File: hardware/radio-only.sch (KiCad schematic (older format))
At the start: 22 parts, among them P1 CONN_2, P2 CONN_2, P3 CONN_4, U3 AT86RF231, Y1 NX3225SA-16MHz-15ppm

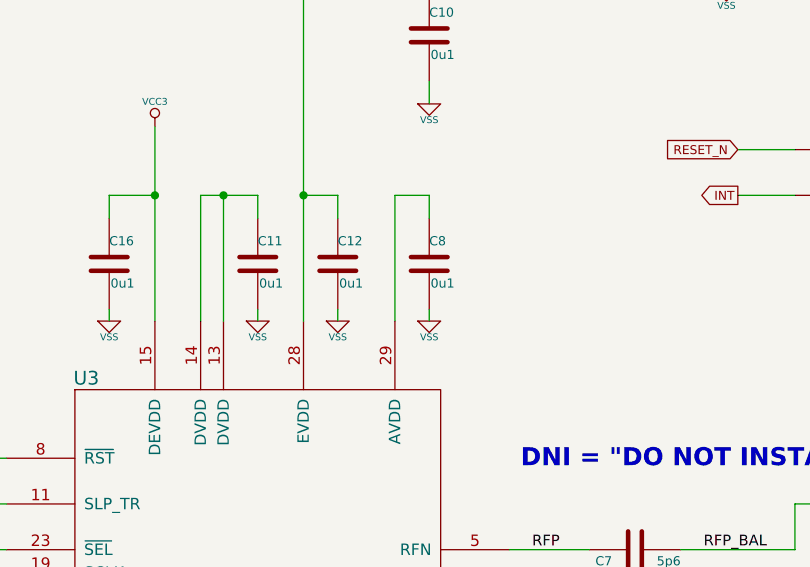
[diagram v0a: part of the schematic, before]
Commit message: Corrections to C8/12 decoupling caps. Should be 0u01, not 0u1 (not critical).
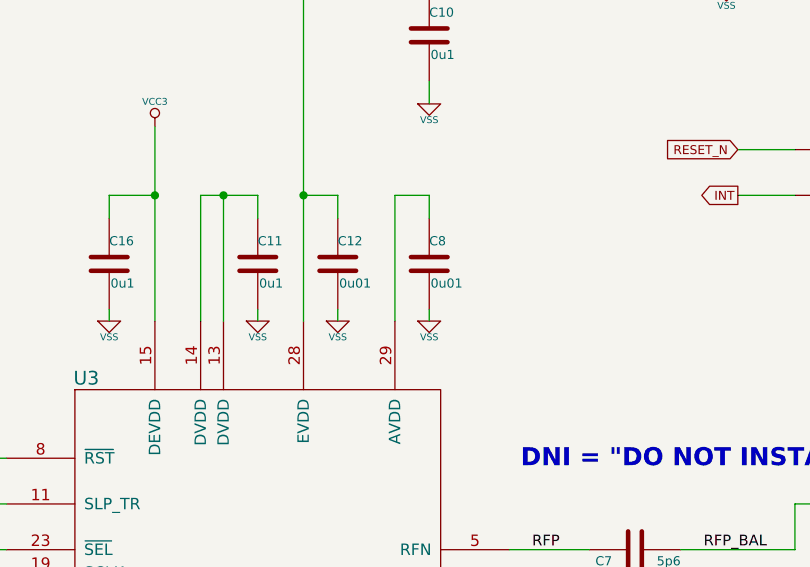
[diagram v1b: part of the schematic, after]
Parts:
- C12, C8: value 0u1 -> 0u01
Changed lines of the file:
@@
 Sheet 1 1
 Title "FREAKDUINO-CHIBI 2.4GHz"
-Date "14 feb 2014"
+Date "3 mar 2014"
 Rev "v1.2"
 Comp "KiCAD version by Gruvin"
@@
 P 4850 2750
 F 0 "C12" H 4850 2850 40  0000 L CNN
-F 1 "0u1" H 4856 2665 40  0000 L CNN
+F 1 "0u01" H 4856 2665 40  0000 L CNN
 F 2 "" H 4888 2600 30  0000 C CNN
 F 3 "" H 4850 2750 60  0000 C CNN
@@
 P 5250 2750
 F 0 "C8" H 5250 2850 40  0000 L CNN
-F 1 "0u1" H 5256 2665 40  0000 L CNN
+F 1 "0u01" H 5256 2665 40  0000 L CNN
 F 2 "" H 5288 2600 30  0000 C CNN
 F 3 "" H 5250 2750 60  0000 C CNN

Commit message: Changed the radio test board a) to lie on its side and b) to include slp_tr (oops).
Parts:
- P2: value CONN_2 -> CONN_3; symbol CONN_2 -> CONN_3
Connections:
- net INT: now also P2.3 (P3); no longer P2.2 (PM)
- net RESET_N: now also P2.2 (PM); no longer P2.1 (P1)
- net SLP_TR: now also P2.1 (P1)
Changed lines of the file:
@@
 $EndComp
 $Comp
-L VCC3 #PWR4
+L VCC3 #PWR01
 U 1 1 51E3885A
 P 3500 1200
-F 0 "#PWR4" H 3500 1340 20  0001 C CNN
+F 0 "#PWR01" H 3500 1340 20  0001 C CNN
 F 1 "VCC3" H 3500 1310 30  0000 C CNN
 F 2 "" H 3500 1200 60  0000 C CNN
@@
 $EndComp
 $Comp
-L VCC3 #PWR7
+L VCC3 #PWR02
 U 1 1 51E383F6
 P 4050 2150
-F 0 "#PWR7" H 4050 2290 20  0001 C CNN
+F 0 "#PWR02" H 4050 2290 20  0001 C CNN
 F 1 "VCC3" H 4050 2260 30  0000 C CNN
 F 2 "" H 4050 2150 60  0000 C CNN
@@
 $EndComp
 $Comp
-L VSS #PWR8
+L VSS #PWR03
 U 1 1 51E38434
 P 4500 3000
-F 0 "#PWR8" H 4500 3000 30  0001 C CNN
+F 0 "#PWR03" H 4500 3000 30  0001 C CNN
 F 1 "VSS" H 4500 2930 30  0000 C CNN
 F 2 "" H 4500 3000 60  0000 C CNN
@@
 $EndComp
 $Comp
-L VSS #PWR10
+L VSS #PWR04
 U 1 1 51E3856B
 P 4850 3000
-F 0 "#PWR10" H 4850 3000 30  0001 C CNN
+F 0 "#PWR04" H 4850 3000 30  0001 C CNN
 F 1 "VSS" H 4850 2930 30  0000 C CNN
 F 2 "" H 4850 3000 60  0000 C CNN
@@
 $EndComp
 $Comp
-L VSS #PWR12
+L VSS #PWR05
 U 1 1 51E3859B
 P 5250 3000
-F 0 "#PWR12" H 5250 3000 30  0001 C CNN
+F 0 "#PWR05" H 5250 3000 30  0001 C CNN
 F 1 "VSS" H 5250 2930 30  0000 C CNN
 F 2 "" H 5250 3000 60  0000 C CNN
@@
 $EndComp
 $Comp
-L VSS #PWR6
+L VSS #PWR06
 U 1 1 51E385BF
 P 3850 6050
-F 0 "#PWR6" H 3850 6050 30  0001 C CNN
+F 0 "#PWR06" H 3850 6050 30  0001 C CNN
 F 1 "VSS" H 3850 5980 30  0000 C CNN
 F 2 "" H 3850 6050 60  0000 C CNN
@@
 $EndComp
 $Comp
-L VSS #PWR9
+L VSS #PWR07
 U 1 1 51E385C5
 P 4600 6050
-F 0 "#PWR9" H 4600 6050 30  0001 C CNN
+F 0 "#PWR07" H 4600 6050 30  0001 C CNN
 F 1 "VSS" H 4600 5980 30  0000 C CNN
 F 2 "" H 4600 6050 60  0000 C CNN
@@
 $EndComp
 $Comp
-L VSS #PWR1
+L VSS #PWR08
 U 1 1 51E39377
 P 1050 5850
-F 0 "#PWR1" H 1050 5850 30  0001 C CNN
+F 0 "#PWR08" H 1050 5850 30  0001 C CNN
 F 1 "VSS" H 1050 5780 30  0000 C CNN
 F 2 "" H 1050 5850 60  0000 C CNN
@@
 $EndComp
 $Comp
-L VSS #PWR2
+L VSS #PWR09
 U 1 1 51E3937D
 P 1850 5850
-F 0 "#PWR2" H 1850 5850 30  0001 C CNN
+F 0 "#PWR09" H 1850 5850 30  0001 C CNN
 F 1 "VSS" H 1850 5780 30  0000 C CNN
 F 2 "" H 1850 5850 60  0000 C CNN
@@
 $EndComp
 $Comp
-L VCC3 #PWR3
+L VCC3 #PWR010
 U 1 1 51E39903
 P 2950 2500
-F 0 "#PWR3" H 2950 2640 20  0001 C CNN
+F 0 "#PWR010" H 2950 2640 20  0001 C CNN
 F 1 "VCC3" H 2950 2610 30  0000 C CNN
 F 2 "" H 2950 2500 60  0000 C CNN
@@
 ANT
 $Comp
-L VSS #PWR17
+L VSS #PWR011
 U 1 1 51E3A542
 P 8500 4500
-F 0 "#PWR17" H 8500 4500 30  0001 C CNN
+F 0 "#PWR011" H 8500 4500 30  0001 C CNN
 F 1 "VSS" H 8500 4430 30  0000 C CNN
 F 2 "" H 8500 4500 60  0000 C CNN
@@
 $EndComp
 $Comp
-L VSS #PWR18
+L VSS #PWR012
 U 1 1 51E3A548
 P 9400 4500
-F 0 "#PWR18" H 9400 4500 30  0001 C CNN
+F 0 "#PWR012" H 9400 4500 30  0001 C CNN
 F 1 "VSS" H 9400 4430 30  0000 C CNN
 F 2 "" H 9400 4500 60  0000 C CNN
@@
 $EndComp
 $Comp
-L VSS #PWR16
+L VSS #PWR013
 U 1 1 51E3A80A
 P 7400 4750
-F 0 "#PWR16" H 7400 4750 30  0001 C CNN
+F 0 "#PWR013" H 7400 4750 30  0001 C CNN
 F 1 "VSS" H 7400 4680 30  0000 C CNN
 F 2 "" H 7400 4750 60  0000 C CNN
@@
 $EndComp
 $Comp
-L VSS #PWR19
+L VSS #PWR014
 U 1 1 51E3A9B9
 P 10200 4600
-F 0 "#PWR19" H 10200 4600 30  0001 C CNN
+F 0 "#PWR014" H 10200 4600 30  0001 C CNN
 F 1 "VSS" H 10200 4530 30  0000 C CNN
 F 2 "" H 10200 4600 60  0000 C CNN
@@
 $EndComp
 $Comp
-L VSS #PWR5
+L VSS #PWR015
 U 1 1 51E3ADC4
 P 3850 3000
-F 0 "#PWR5" H 3850 3000 30  0001 C CNN
+F 0 "#PWR015" H 3850 3000 30  0001 C CNN
 F 1 "VSS" H 3850 2930 30  0000 C CNN
 F 2 "" H 3850 3000 60  0000 C CNN
@@
 $EndComp
 $Comp
-L VSS #PWR15
+L VSS #PWR016
 U 1 1 51E79531
 P 7400 3650
-F 0 "#PWR15" H 7400 3650 30  0001 C CNN
+F 0 "#PWR016" H 7400 3650 30  0001 C CNN
 F 1 "VSS" H 7400 3580 30  0000 C CNN
 F 2 "" H 7400 3650 60  0000 C CNN
@@
 	5250 1950 5250 2050
 $Comp
-L VSS #PWR11
+L VSS #PWR017
 U 1 1 51E39C73
 P 5250 2050
-F 0 "#PWR11" H 5250 2050 30  0001 C CNN
+F 0 "#PWR017" H 5250 2050 30  0001 C CNN
 F 1 "VSS" H 5250 1980 30  0000 C CNN
 F 2 "" H 5250 2050 60  0000 C CNN
@@
 $EndComp
 $Comp
-L CONN_2 P2
+L CONN_3 P2
 U 1 1 52FE909C
 P 7200 2350
 F 0 "P2" V 7150 2350 40  0000 C CNN
-F 1 "CONN_2" V 7250 2350 40  0000 C CNN
+F 1 "CONN_3" V 7250 2350 40  0000 C CNN
 F 2 "" H 7200 2350 60  0000 C CNN
 F 3 "" H 7200 2350 60  0000 C CNN
@@
 $EndComp
 $Comp
-L VCC3 #PWR13
+L VCC3 #PWR018
 U 1 1 52FE90BB
 P 6550 1150
-F 0 "#PWR13" H 6550 1290 20  0001 C CNN
+F 0 "#PWR018" H 6550 1290 20  0001 C CNN
 F 1 "VCC3" H 6550 1260 30  0000 C CNN
 F 2 "" H 6550 1150 60  0000 C CNN
@@
 $EndComp
 $Comp
-L VSS #PWR14
+L VSS #PWR019
 U 1 1 52FE90C1
 P 6550 1550
-F 0 "#PWR14" H 6550 1550 30  0001 C CNN
+F 0 "#PWR019" H 6550 1550 30  0001 C CNN
 F 1 "VSS" H 6550 1480 30  0000 C CNN
 F 2 "" H 6550 1550 60  0000 C CNN
@@
 Wire Wire Line
 	6550 1200 6850 1200
-Text GLabel 6600 2250 0    39   Input ~ 0
+Text GLabel 6600 2350 0    39   Input ~ 0
 RESET_N
 Text GLabel 6600 2450 0    39   Output ~ 0
 INT
 Wire Wire Line
-	6600 2450 6850 2450
+	6600 2350 6850 2350
 Wire Wire Line
 	6600 2250 6850 2250
@@
 Wire Wire Line
 	8050 1600 8250 1600
+Text GLabel 6600 2250 0    39   Output ~ 0
+SLP_TR
+Wire Wire Line
+	6600 2450 6850 2450
 $EndSCHEMATC
